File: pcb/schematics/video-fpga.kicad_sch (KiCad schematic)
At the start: 60 parts, among them J5 Conn_01x06, J6 Conn_01x06, U4 LCMXO2-7000HC-4TG144C, X1 ASV-xxxMHz

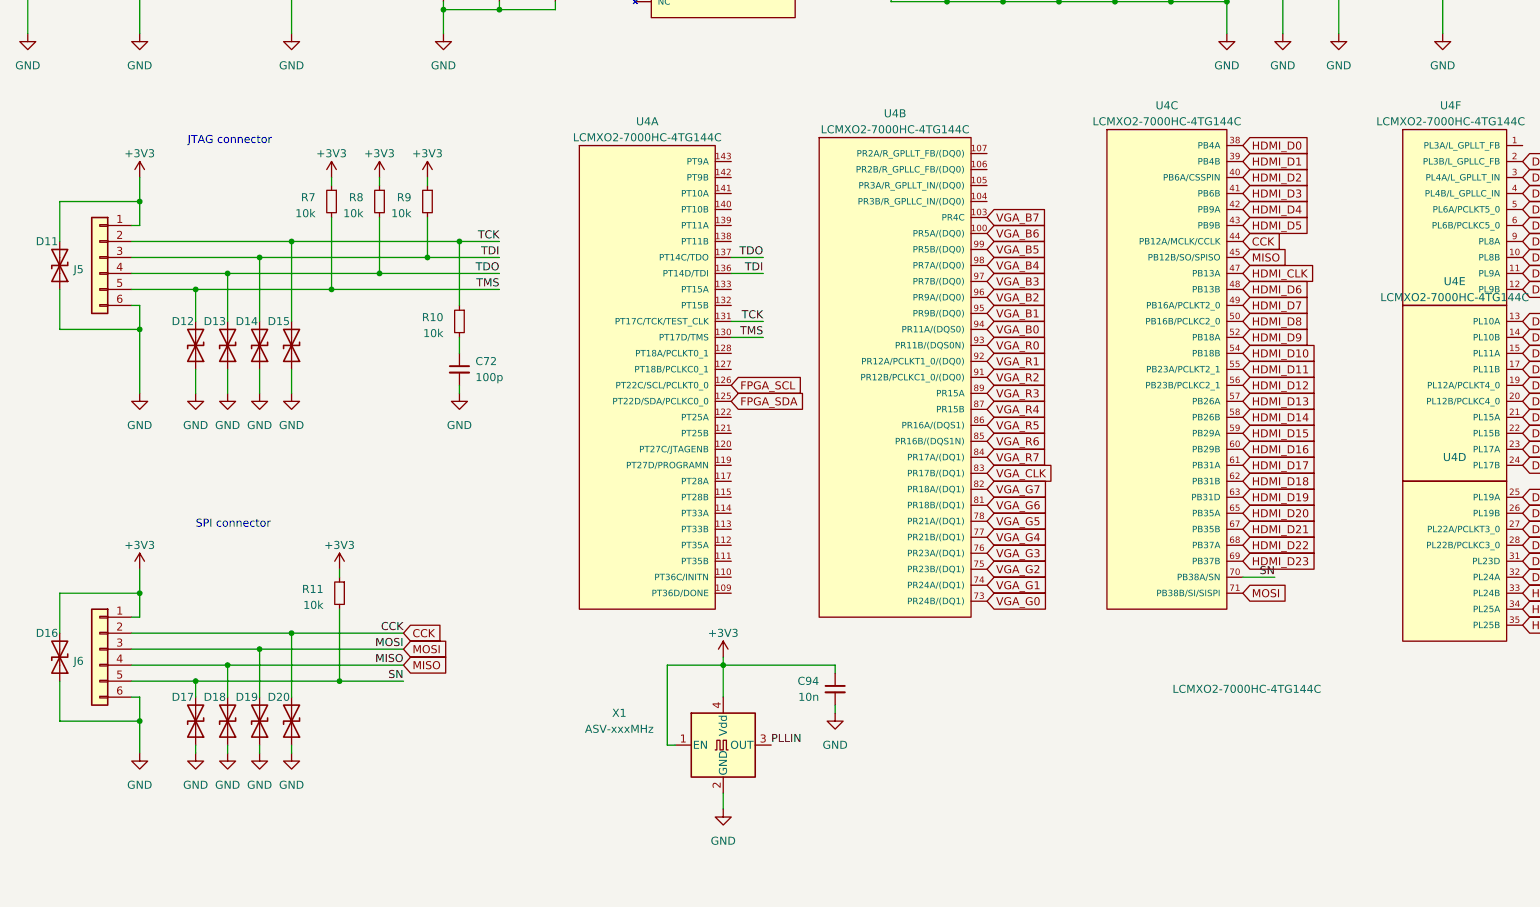
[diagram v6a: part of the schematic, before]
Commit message: add a unified programming connector
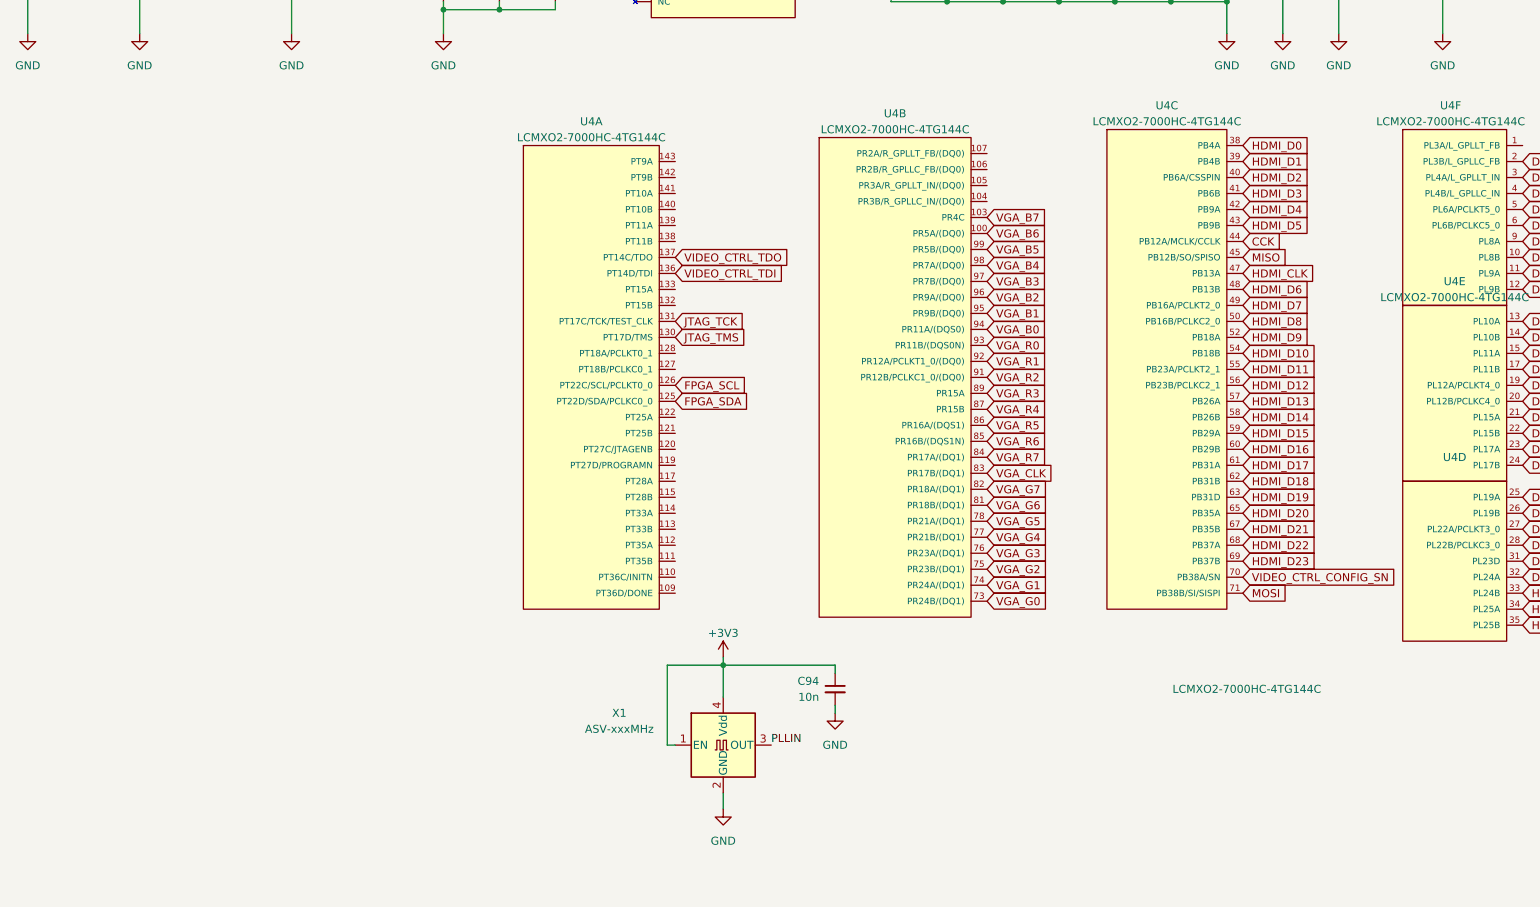
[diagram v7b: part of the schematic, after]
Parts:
- removed C72: 100p, Capacitor_SMD:C_0402_1005Metric, symbol Device:C_Small
- removed D11, D12, D13, D14, D15, D16, D17, D18, D19, D20: D_TVS, Diode_SMD:D_0603_1608Metric, symbol Device:D_TVS
- removed J5, J6: Conn_01x06, Connector:Tag-Connect_TC2030-IDC-NL_2x03_P1.27mm_Vertical, symbol Connector_Generic:Conn_01x06
- removed R10, R11, R7, R8, R9: 10k, Resistor_SMD:R_0603_1608Metric, symbol Device:R_Small
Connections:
- net SN renamed VIDEO_CTRL_CONFIG_SN
- net TCK renamed JTAG_TCK
- net TDI renamed VIDEO_CTRL_TDI
- net TDO renamed VIDEO_CTRL_TDO
- net TMS renamed JTAG_TMS
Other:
- note removed: "JTAG connector"
- note removed: "SPI connector"
- moved on the sheet: U4A

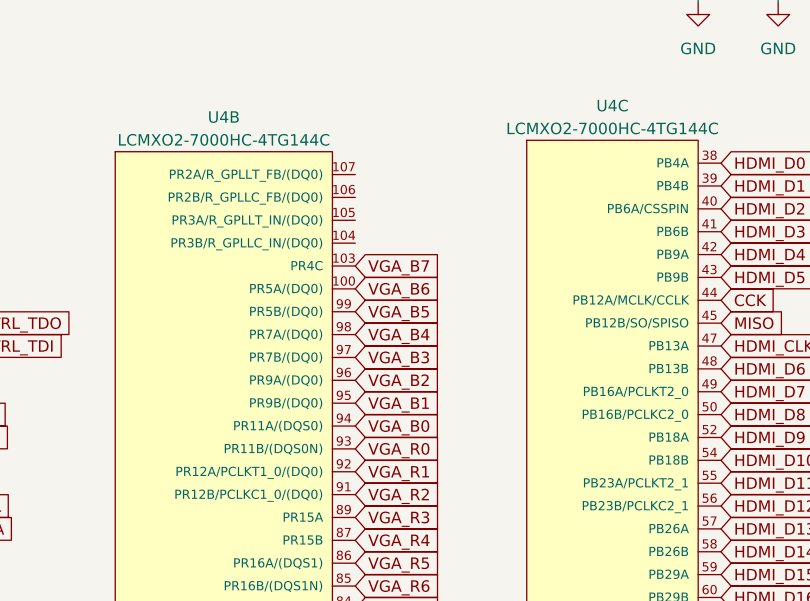
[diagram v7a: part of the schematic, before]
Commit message: add traces to the vga frontend
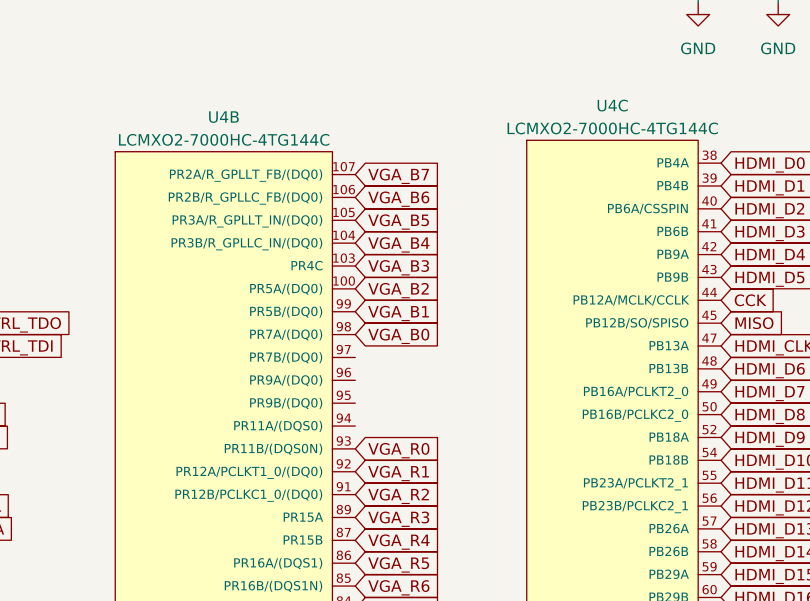
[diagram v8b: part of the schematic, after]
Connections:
- net VGA_B0: now also U4.98 (PR7A/(DQ0)); no longer U4.94 (PR11A/(DQS0))
- net VGA_B1: now also U4.99 (PR5B/(DQ0)); no longer U4.95 (PR9B/(DQ0))
- net VGA_B2: now also U4.100 (PR5A/(DQ0)); no longer U4.96 (PR9A/(DQ0))
- net VGA_B3: now also U4.103 (PR4C); no longer U4.97 (PR7B/(DQ0))
- net VGA_B4: now also U4.104 (PR3B/R_GPLLC_IN/(DQ0)); no longer U4.98 (PR7A/(DQ0))
- net VGA_B5: now also U4.105 (PR3A/R_GPLLT_IN/(DQ0)); no longer U4.99 (PR5B/(DQ0))
- net VGA_B6: now also U4.106 (PR2B/R_GPLLC_FB/(DQ0)); no longer U4.100 (PR5A/(DQ0))
- net VGA_B7: now also U4.107 (PR2A/R_GPLLT_FB/(DQ0)); no longer U4.103 (PR4C)
